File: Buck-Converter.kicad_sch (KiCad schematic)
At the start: 0 parts

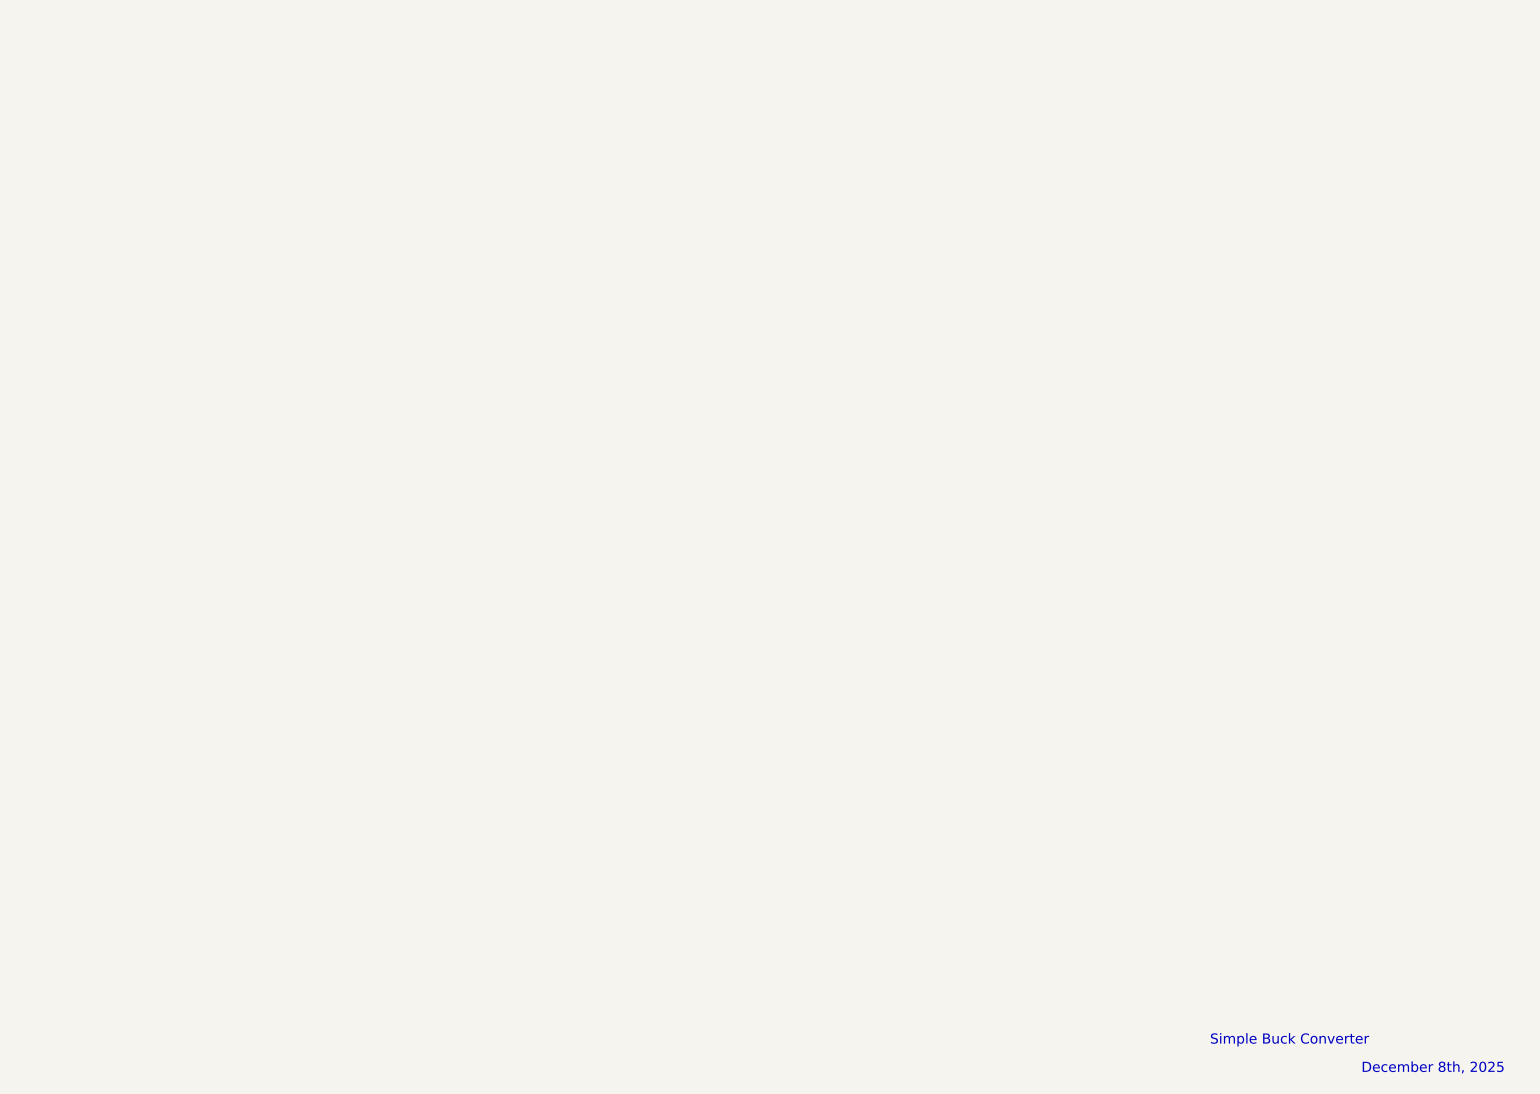
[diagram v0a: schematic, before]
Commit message: Created template circuit for Buck Converter
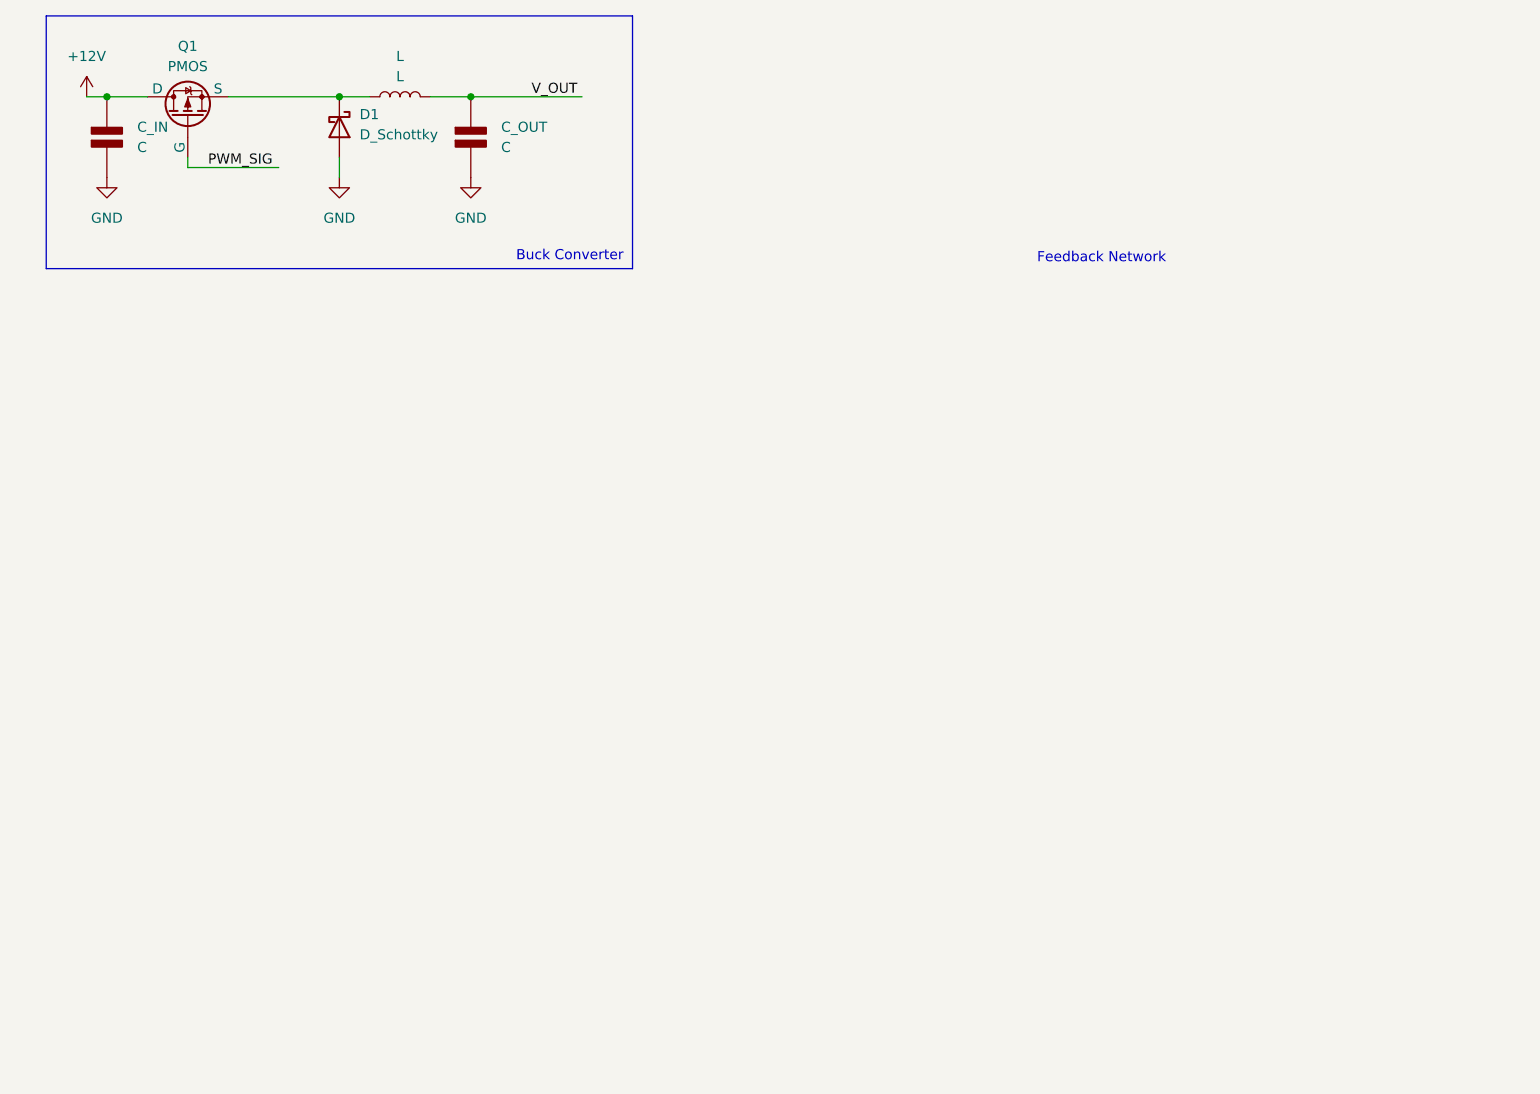
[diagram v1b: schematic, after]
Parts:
- added C_IN, C_OUT: C, symbol PCM_Elektuur:C
- added D1: D_Schottky, symbol Device:D_Schottky
- added L: L, symbol Device:L
- added Q1: PMOS, symbol Simulation_SPICE:PMOS
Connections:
- new net: D1.1 (K), L.1, Q1.3 (S)
- new net +12V: C_IN.1 (+), Q1.1 (D)
- new net GND: C_IN.2 (-), C_OUT.2 (-), D1.2 (A)
- new net PWM_SIG: Q1.2 (G)
- new net V_OUT: C_OUT.1 (+), L.2
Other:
- note added: "Buck Converter"
- note added: "Feedback Network"
- note removed: "December 8th, 2025"
- note removed: "Simple Buck Converter"
- title: (none) -> Simple Buck Converter

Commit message: Added voltage regulator
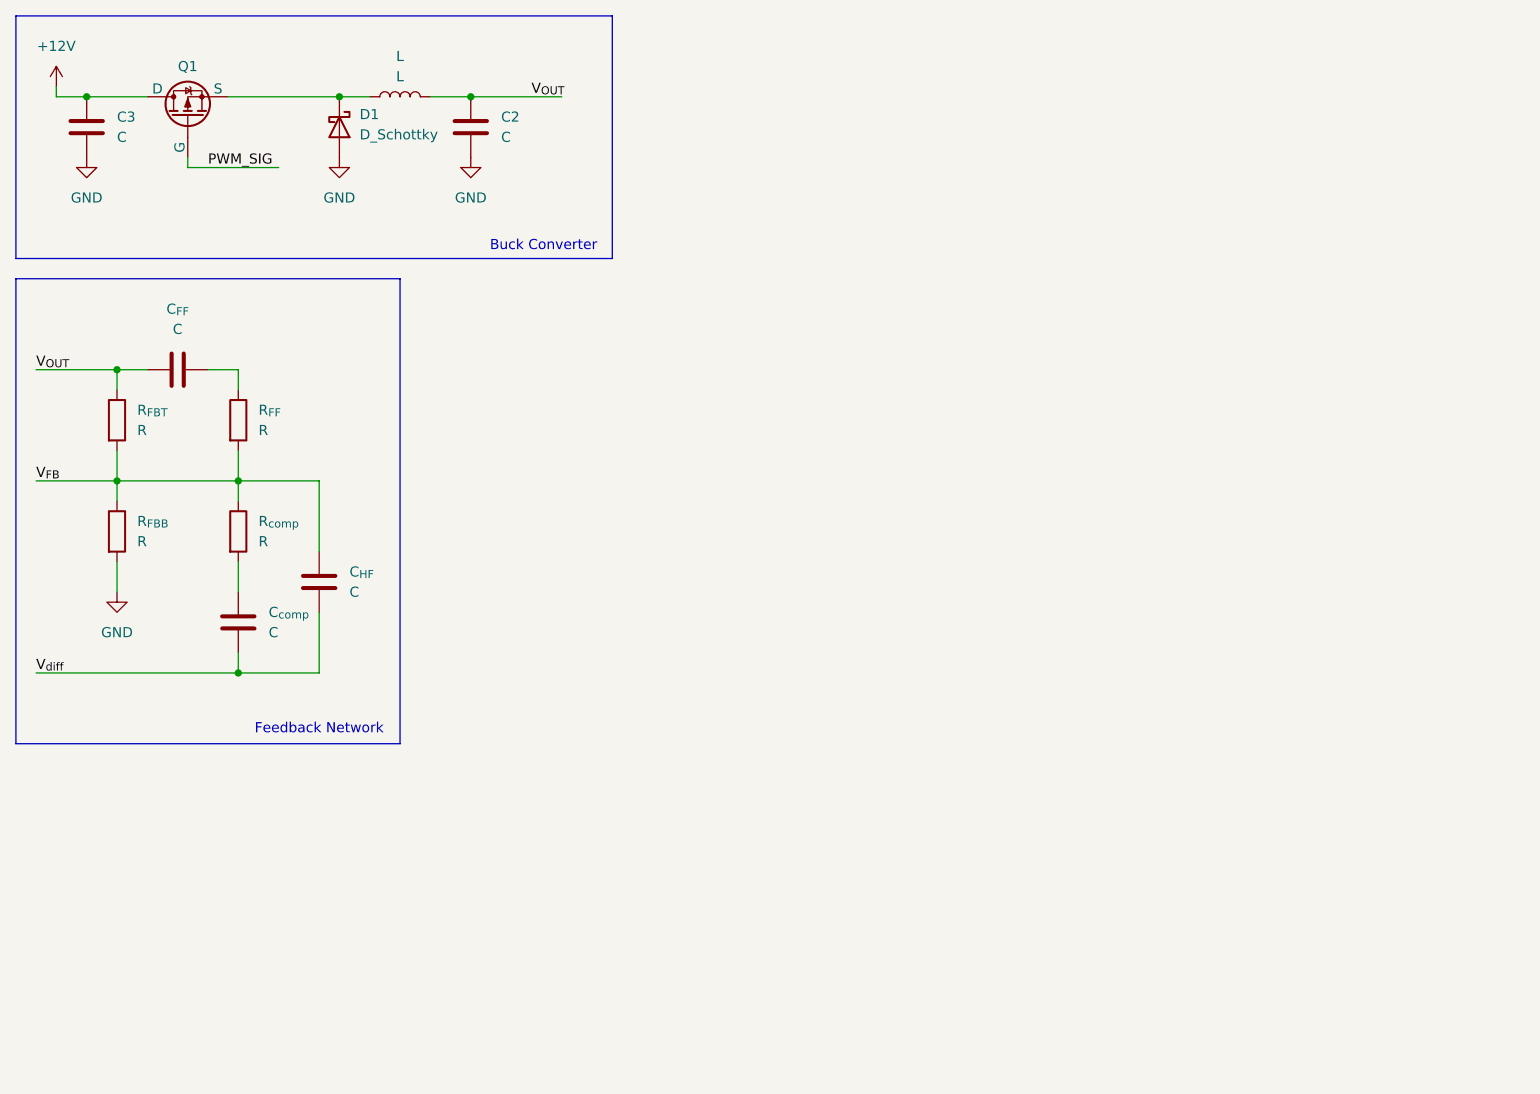
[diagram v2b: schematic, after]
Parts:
- removed C_IN, C_OUT: C, symbol PCM_Elektuur:C
- added C2, C3, C_{FF}, C_{HF}, C_{comp}: C, symbol Device:C
- added R_{FBB}, R_{FBT}, R_{FF}, R_{comp}: R, symbol Device:R
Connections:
- net +12V: now also C3.1
- net GND: now also C2.2, C3.2, R_{FBB}.2
- net V_OUT renamed V_{OUT}
- net V_{OUT}: now also C2.1, C_{FF}.1, R_{FBT}.1
- new net: C_{comp}.2, R_{comp}.2
- new net: C_{FF}.2, R_{FF}.1
- new net V_{FB}: C_{HF}.2, R_{FBB}.1, R_{FBT}.2, R_{FF}.2, R_{comp}.1
- new net V_{diff}: C_{HF}.1, C_{comp}.1
